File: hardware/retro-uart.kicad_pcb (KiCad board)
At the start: 2 copper layers, 17.4 x 51.4 mm, 17 parts, among them J1 DIP, U1 TL16C750E, U2 MAX7375AXR805, U3 74LVC1G10, U4 74LVC3G04, U5 74LVC2G02

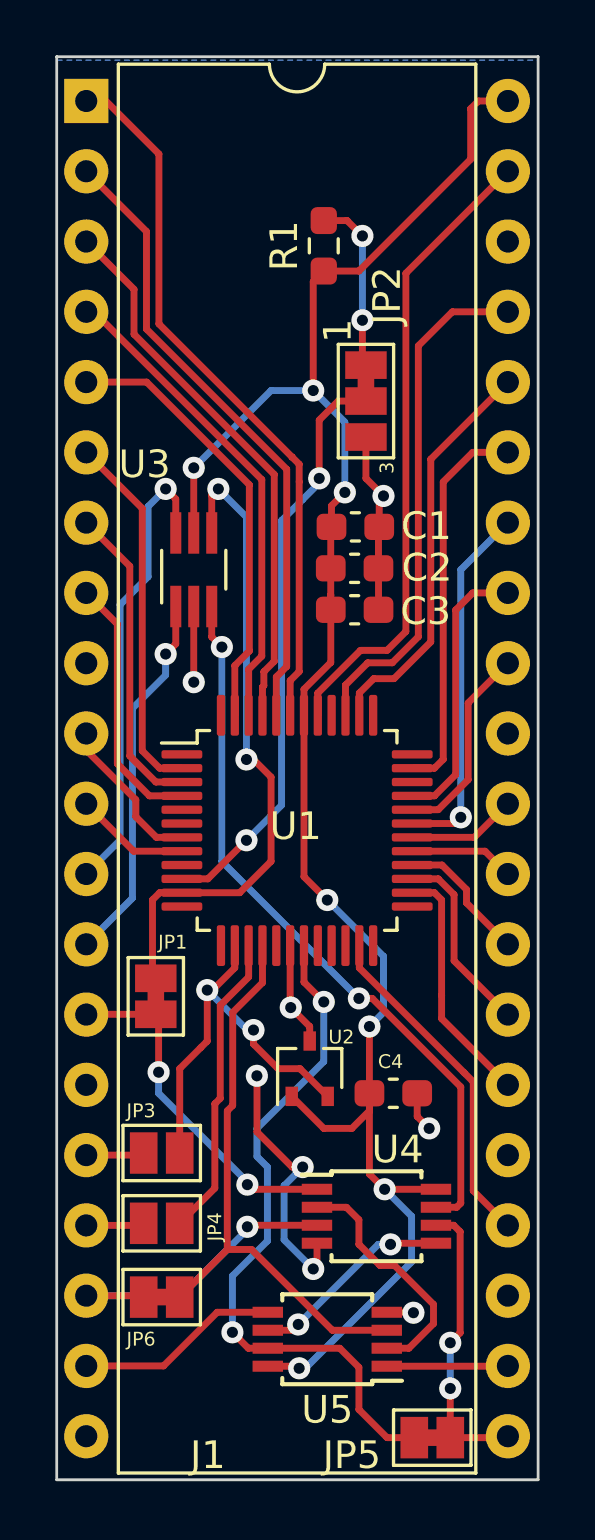
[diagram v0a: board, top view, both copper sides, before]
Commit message: Fix courtyard issues.
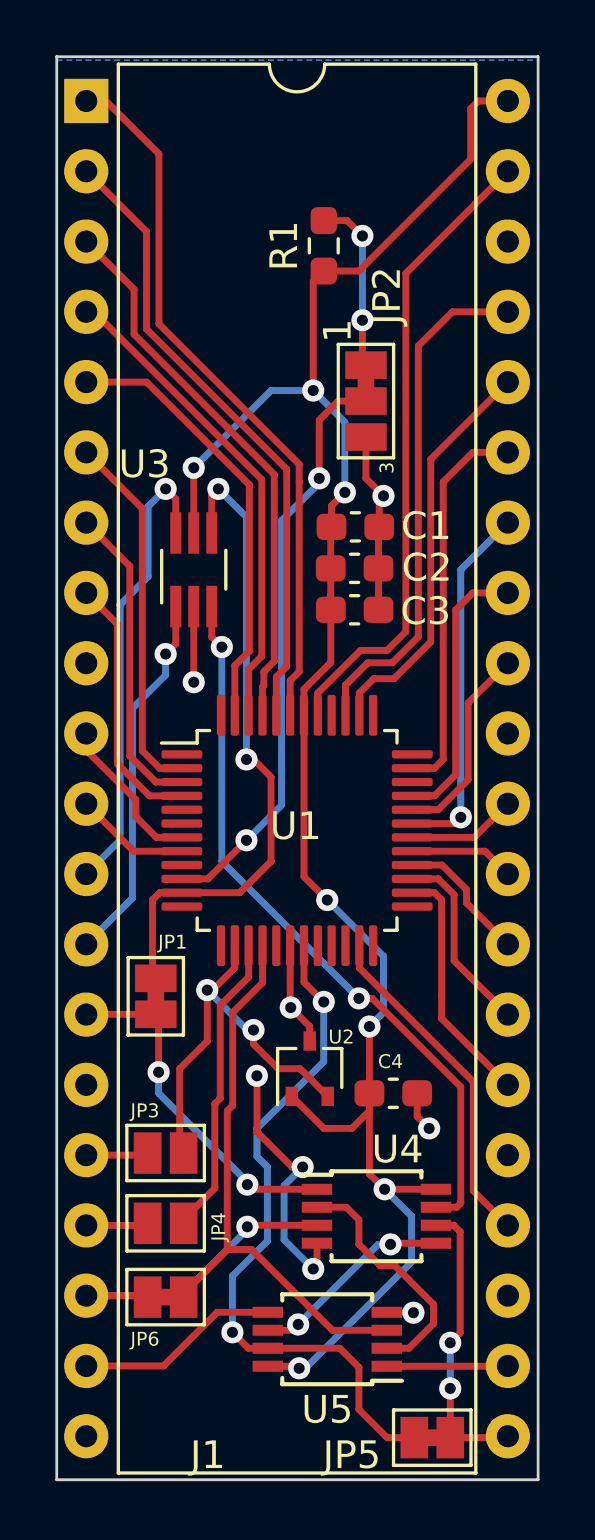
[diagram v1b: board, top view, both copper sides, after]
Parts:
- moved JP3 0.14 mm to (24.4, 57.4)
- moved JP4 0.14 mm to (24.4, 59.9)
- moved JP6 0.14 mm to (24.4, 62.6)
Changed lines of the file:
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@@
     (fp_line (start 1.16 49.59) (end 14.08 49.59) (layer "F.SilkS") (width 0.12))
     (fp_arc (start 8.62 -1.33) (mid 7.62 -0.33) (end 6.62 -1.33) (layer "F.SilkS") (width 0.12))
-    (fp_line (start -1.05 49.8) (end 16.3 49.8) (layer "F.CrtYd") (width 0.05))
-    (fp_line (start 16.3 -1.55) (end -1.05 -1.55) (layer "F.CrtYd") (width 0.05))
-    (fp_line (start 16.3 49.8) (end 16.3 -1.55) (layer "F.CrtYd") (width 0.05))
-    (fp_line (start -1.05 -1.55) (end -1.05 49.8) (layer "F.CrtYd") (width 0.05))
+    (fp_line (start 1.165 49.53) (end -1.165 49.53) (layer "F.CrtYd") (width 0.05))
+    (fp_line (start -1.165 -1.27) (end -1.165 49.53) (layer "F.CrtYd") (width 0.05))
+    (fp_line (start 16.3 -1.27) (end 13.97 -1.27) (layer "F.CrtYd") (width 0.05))
+    (fp_line (start 16.3 49.53) (end 16.3 -1.27) (layer "F.CrtYd") (width 0.05))
+    (fp_line (start 16.3 49.53) (end 14.075 49.53) (layer "F.CrtYd") (width 0.05))
+    (fp_line (start 1.165 -1.27) (end 1.165 49.53) (layer "F.CrtYd") (width 0.05))
+    (fp_line (start 1.165 -1.27) (end -1.165 -1.27) (layer "F.CrtYd") (width 0.05))
+    (fp_line (start 13.97 -1.27) (end 13.97 49.53) (layer "F.CrtYd") (width 0.05))
     (fp_line (start 0.255 49.53) (end 0.255 -0.27) (layer "F.Fab") (width 0.1))
     (fp_line (start 0.255 -0.27) (end 1.255 -1.27) (layer "F.Fab") (width 0.1))
@@
   )
   (footprint "Jumper:SolderJumper-2_P1.3mm_Open_Pad1.0x1.5mm" (layer "F.Cu")
-    (at 24.242 59.944)
+    (at 24.384 59.944)
     (descr "SMD Solder Jumper, 1x1.5mm Pads, 0.3mm gap, open")
     (tags "solder jumper open")
@@
   )
   (footprint "Jumper:SolderJumper-2_P1.3mm_Bridged_Pad1.0x1.5mm" (layer "F.Cu")
-    (at 24.242 62.611)
+    (at 24.384 62.611)
     (descr "SMD Solder Jumper, 1x1.5mm Pads, 0.3mm gap, bridged with 1 copper strip")
     (tags "net tie solder jumper bridged")
@@
   )
   (footprint "Jumper:SolderJumper-2_P1.3mm_Open_Pad1.0x1.5mm" (layer "F.Cu")
-    (at 24.242 57.404)
+    (at 24.384 57.404)
     (descr "SMD Solder Jumper, 1x1.5mm Pads, 0.3mm gap, open")
     (tags "solder jumper open")
@@
   (segment (start 33.323609 63.16) (end 33.340281 63.176672) (width 0.25) (layer "F.Cu") (net 3))
   (segment (start 32.376 63.16) (end 33.323609 63.16) (width 0.25) (layer "F.Cu") (net 3))
-  (segment (start 32.1034 34.7726) (end 32.1034 34.6964) (width 0.25) (layer "F.Cu") (net 3))
   (segment (start 32.078 36.2734) (end 32.0758 36.2712) (width 0.25) (layer "F.Cu") (net 3))
   (segment (start 32.0758 36.2712) (end 32.0758 34.8002) (width 0.25) (layer "F.Cu") (net 3))
@@
   (segment (start 29.591 53.356) (end 29.591 52.832) (width 0.25) (layer "F.Cu") (net 3))
   (segment (start 33.475 55.245) (end 33.475 56.081) (width 0.25) (layer "F.Cu") (net 3))
-  (segment (start 32.0758 34.8002) (end 32.1034 34.7726) (width 0.25) (layer "F.Cu") (net 3))
   (segment (start 32.078 37.7698) (end 32.078 36.2734) (width 0.25) (layer "F.Cu") (net 3))
   (segment (start 29.591 52.832) (end 28.9052 52.1462) (width 0.25) (layer "F.Cu") (net 3))
@@
   (segment (start 29.21 33.147) (end 29.21 32.506416) (width 0.25) (layer "F.Cu") (net 40))
   (segment (start 22.225 19.3802) (end 21.5138 19.3802) (width 0.25) (layer "F.Cu") (net 40))
-  (segment (start 28.958792 32.255208) (end 28.946396 32.242812) (width 0.25) (layer "F.Cu") (net 40))
   (segment (start 28.8838 40.3312) (end 29.21 40.005) (width 0.25) (layer "F.Cu") (net 40))
   (segment (start 24.141 21.2962) (end 22.225 19.3802) (width 0.25) (layer "F.Cu") (net 40))
